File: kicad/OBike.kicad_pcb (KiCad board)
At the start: 4 copper layers, 64 x 99.2 mm, 60 parts, among them J2 Micro_SD_Card_Det1, J3 Conn_01x02, SW1 5_position_tactile, U1 DPS368XTSA1, U2 DS3231M, U3 MCP23017_SO, U4 74HC14, U5 Seeed Studio XIAO SAMD21, U6 MAX40200AUK, U7 L86-M33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

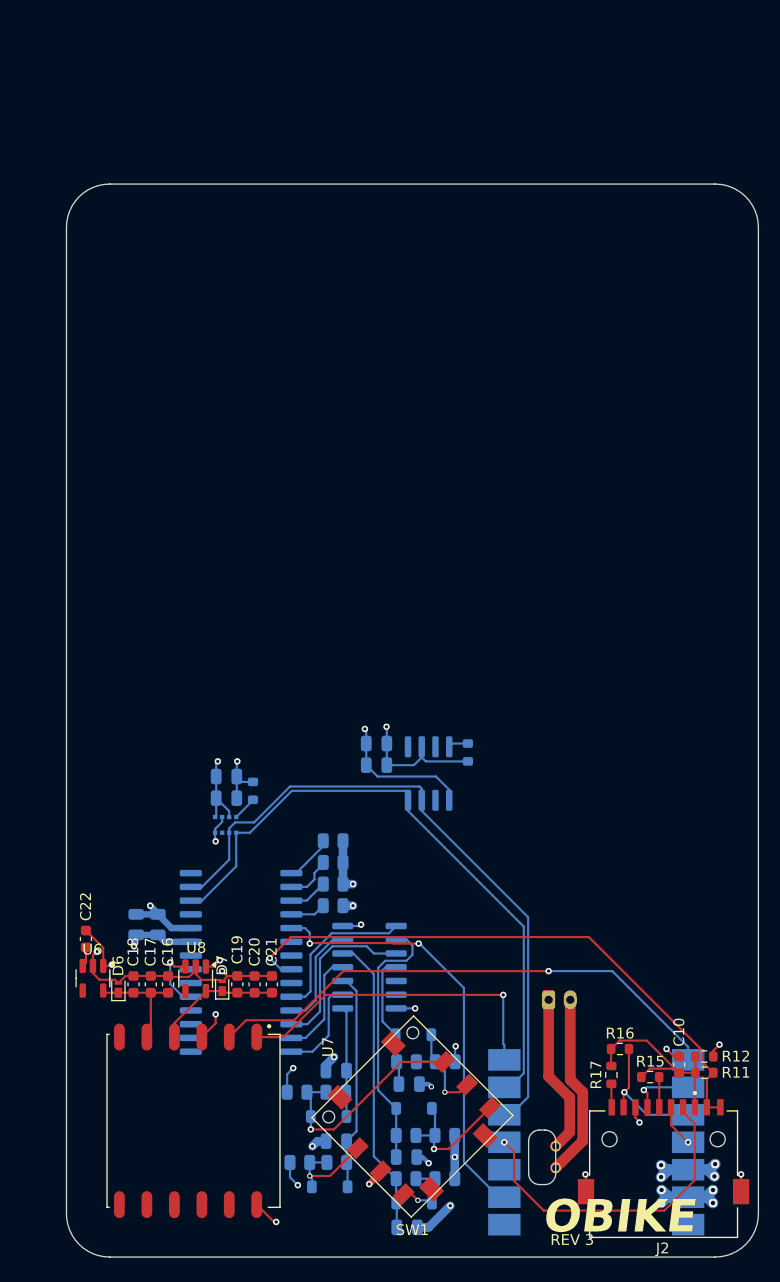
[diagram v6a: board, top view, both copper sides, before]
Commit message: rev 3 pcb
- quectel gps
- u.fl antenae conn
- aux power switch
- flash chip
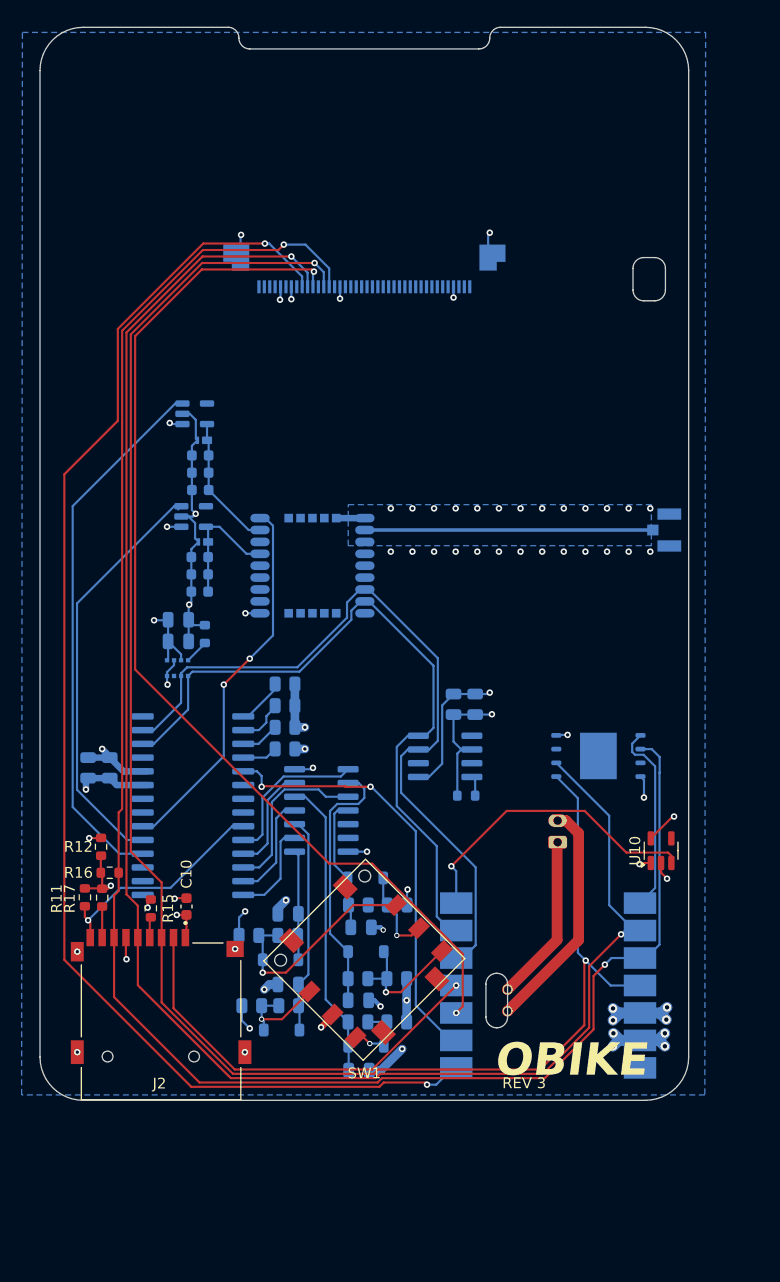
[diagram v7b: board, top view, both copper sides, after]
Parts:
- removed C22: 10uF, Capacitor_SMD:C_0603_1608Metric
- added J1: 62684-402100ALF, amphenol:AMPHENOL_62684-402100ALF, B.Cu at (148.1, 57.4)
- added J5: U.FL-R-SMT-1_10_, Hirose:HRS_U.FL-R-SMT-1_10_, B.Cu at (176.3, 83.5)
- added U10: MAX40200AUK, Package_TO_SOT_SMD:SOT-23-5, F.Cu at (175.5, 113.2)
- added U9: W25N01GVZEIG_TR, windbond:SON127P800X600X80-9N, B.Cu at (169.7, 104.4)
- C16, C17, C18, C19, C20, C21, D6, D7, U6, U8: moved to B.Cu
- J2: footprint CUI-devices:CUI_MSD-11-A -> CUI:CUI_MSD-4-A
- U7: value L86-M33 -> LC76G; footprint quectel:L86-M33 -> quectel:XCVR_LC76G; moved to B.Cu
- moved R11 59.6 mm to (122.2, 117.5), turned to -90 degrees
- moved R12 59.1 mm to (123.7, 112.8), turned to -90 degrees
- moved U7 52.6 mm to (143.2, 86.8), turned to 0 degrees
- moved U8 52.3 mm to (132.4, 72.8), turned to 0 degrees
- moved D7 50.7 mm to (133.2, 75.2), turned to 180 degrees
- moved R16 49.9 mm to (124.5, 115.2)
- moved R17 49.9 mm to (123.8, 117.5)
- moved C19 49.0 mm to (132.9, 76.6), turned to 180 degrees
- moved R15 48.8 mm to (128.3, 118.5), turned to -90 degrees
- moved J2 48.6 mm to (129.2, 128.9)
- moved C10 47.9 mm to (131.6, 118.3)
- moved C20 47.6 mm to (132.9, 78.2), turned to 180 degrees
- moved C21 46.2 mm to (132.9, 79.8), turned to 180 degrees
- moved U6 43.7 mm to (132.3, 82.2), turned to 0 degrees
- moved D6 42.2 mm to (133.3, 84.6), turned to 180 degrees
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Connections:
- C3 pad 1: 3V3 -> AUX_3V3
- C4 pad 1: 3V3 -> AUX_3V3
- R11 pad 2: DET -> CD
- R12 pad 1: 3V3 -> AUX_3V3
- U1 pad 6: 3V3 -> AUX_3V3
- U1 pad 8: 3V3 -> AUX_3V3
- U3 pad 22: DET -> unconnected-(U3-GPA1-Pad22)
- U3 pad 23: unconnected-(U3-GPA2-Pad23) -> CD
- U3 pad 4: unconnected-(U3-GPB3-Pad4) -> GPS_EN
- U3 pad 5: GPS_EN -> GPS_BKP
- U5 pad 7: TX -> AUX_EN
- U5 pad 8: RX -> FL_CS
- U6 pad 3: Net-(U6-EN) -> GPS_BKP
- U7 pad 1: TX -> GND
- U7 pad 10: unconnected-(U7-~{RESET}-Pad10) -> GND
- U7 pad 11: unconnected-(U7-EX_ANT-Pad11) -> ANT
- U7 pad 2: RX -> unconnected-(U7-TXD-Pad2)
- U7 pad 3: GND -> unconnected-(U7-RXD-Pad3)
- U7 pad 4: GPS_VCC -> unconnected-(U7-1PPS-Pad4)
- U7 pad 5: GPS_V_BKP -> unconnected-(U7-~{AP_REQ}-Pad5)
- U7 pad 6: unconnected-(U7-1PPS-Pad6) -> GPS_V_BKP
- U7 pad 8: unconnected-(U7-AADET_N-Pad8) -> GPS_VCC
- U7 pad 9: (no net) -> GPS_RST
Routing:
- net AUX_3V3: track 0.00 -> 221.4 mm, vias 0 -> 5
- net MISO: track 12.4 -> 168.3 mm, vias 1 -> 2
- net MOSI: track 3.88 -> 159.1 mm, vias 1 -> 2
- net SCK: track 5.98 -> 160.4 mm, vias 1 -> 2
- net SCR_CS: track 0.00 -> 125.0 mm, vias 0 -> 2
- net SCR_DC: track 0.00 -> 98.3 mm, vias 0 -> 2
- net DET: track 54.8 -> 0.00 mm, vias 1 -> 0
- net RX: track 49.4 -> 0.00 mm, vias 1 -> 0
- net GPS_EN: track 5.94 -> 50.2 mm, vias 1 -> 0
- net GPS_BKP: track 0.00 -> 39.0 mm
- net GPS_RST: track 0.00 -> 34.9 mm, vias 0 -> 2
- net TX: track 30.5 -> 0.00 mm, vias 1 -> 0
- net AUX_EN: track 0.00 -> 28.5 mm, vias 0 -> 1
- net ANT: track 0.00 -> 26.6 mm
- net CD: track 0.00 -> 21.1 mm, vias 0 -> 1
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- added copper zone on B.Cu, net GND
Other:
- board size 64 x 99.2 mm -> 60 x 99.2 mm

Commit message: Purchased PCBs
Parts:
- added C13: 0.1uF, Capacitor_SMD:C_0805_2012Metric, B.Cu at (163.8, 101.5)
- added C14: 1.0uF, Capacitor_SMD:C_0805_2012Metric, B.Cu at (161.8, 101.5)
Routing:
- net AUX_3V3: track 221.4 -> 225.5 mm
- net GND: track 95.8 -> 99.5 mm, vias 57 -> 58
- net /BAT-: track 21.6 -> 22.6 mm
- net MISO: track 168.3 -> 167.7 mm
- net /BAT+: track 15.5 -> 16.1 mm
- net 3V3: vias 15 -> 16
